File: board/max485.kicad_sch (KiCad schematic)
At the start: 9 parts, among them U1 MAX485E

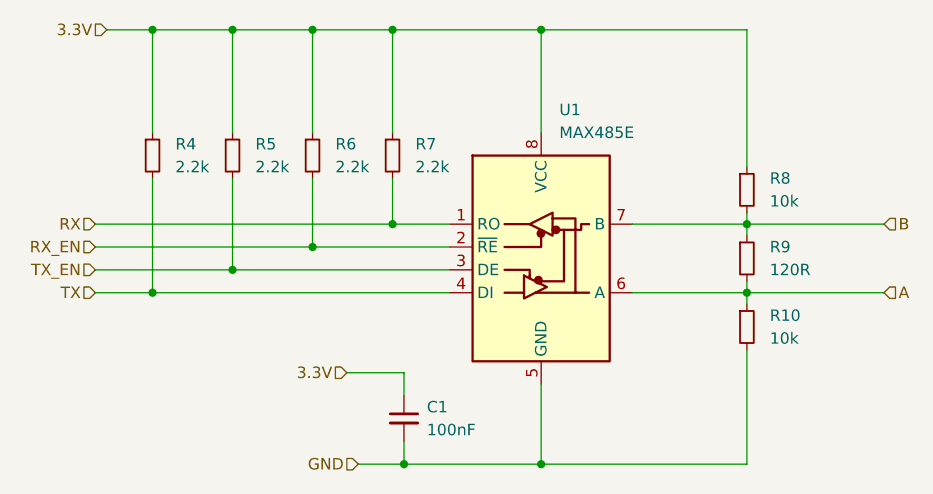
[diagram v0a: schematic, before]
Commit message: changed implementation.kicad_sch to max485.kicad_sch in order to avoid clashing on the name implementation with other edgies in a composition
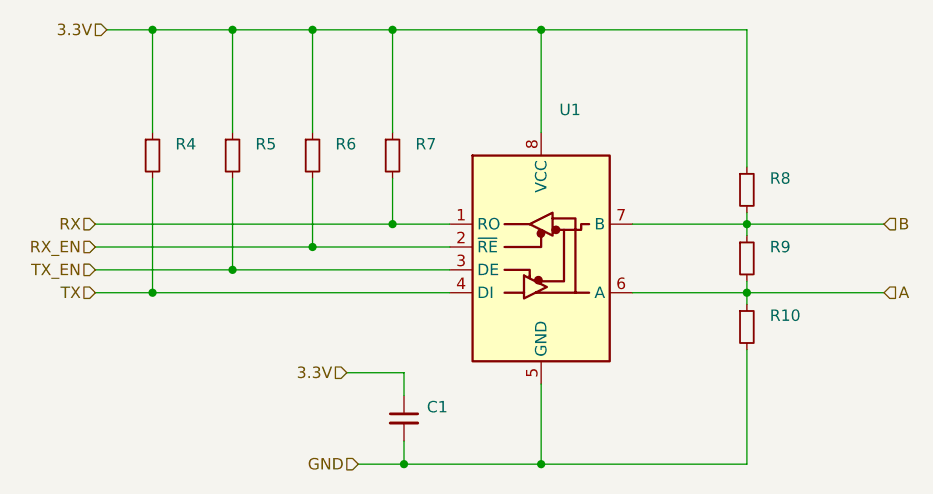
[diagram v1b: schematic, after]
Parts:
- C1: value 100nF -> (none); footprint Resistor_SMD:R_0603_1608Metric -> (none)
- R10, R8: value 10k -> (none); footprint Resistor_SMD:R_0603_1608Metric -> (none)
- R4, R5, R6, R7: value 2.2k -> (none); footprint Resistor_SMD:R_0603_1608Metric -> (none)
- R9: value 120R -> (none); footprint Resistor_SMD:R_0603_1608Metric -> (none)
- U1: value MAX485E -> (none); footprint Package_SO:SO-8_3.9x4.9mm_P1.27mm -> (none)
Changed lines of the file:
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@@
       (effects (font (size 1.27 1.27)) (justify left))
     )
-    (property "Value" "2.2k" (id 1) (at 113.03 91.4399 0)
+    (property "Value" "" (id 1) (at 113.03 91.4399 0)
       (effects (font (size 1.27 1.27)) (justify left))
     )
-    (property "Footprint" "Resistor_SMD:R_0603_1608Metric" (id 2) (at 110.49 90.17 0)
+    (property "Footprint" "" (id 2) (at 110.49 90.17 0)
       (effects (font (size 1.27 1.27)) hide)
     )
@@
       (effects (font (size 1.27 1.27)) (justify left))
     )
-    (property "Value" "100nF" (id 1) (at 123.19 120.6562 0)
+    (property "Value" "" (id 1) (at 123.19 120.6562 0)
       (effects (font (size 1.27 1.27)) (justify left))
     )
-    (property "Footprint" "Resistor_SMD:R_0603_1608Metric" (id 2) (at 120.65 119.38 0)
+    (property "Footprint" "" (id 2) (at 120.65 119.38 0)
       (effects (font (size 1.27 1.27)) hide)
     )
@@
       (effects (font (size 1.27 1.27)) (justify left))
     )
-    (property "Value" "2.2k" (id 1) (at 104.14 91.4399 0)
+    (property "Value" "" (id 1) (at 104.14 91.4399 0)
       (effects (font (size 1.27 1.27)) (justify left))
     )
-    (property "Footprint" "Resistor_SMD:R_0603_1608Metric" (id 2) (at 101.6 90.17 0)
+    (property "Footprint" "" (id 2) (at 101.6 90.17 0)
       (effects (font (size 1.27 1.27)) hide)
     )
@@
       (effects (font (size 1.27 1.27)) (justify left))
     )
-    (property "Value" "120R" (id 1) (at 161.29 102.8699 0)
+    (property "Value" "" (id 1) (at 161.29 102.8699 0)
       (effects (font (size 1.27 1.27)) (justify left))
     )
-    (property "Footprint" "Resistor_SMD:R_0603_1608Metric" (id 2) (at 158.75 101.6 0)
+    (property "Footprint" "" (id 2) (at 158.75 101.6 0)
       (effects (font (size 1.27 1.27)) hide)
     )
@@
       (effects (font (size 1.27 1.27)) (justify left))
     )
-    (property "Value" "10k" (id 1) (at 161.29 110.4899 0)
+    (property "Value" "" (id 1) (at 161.29 110.4899 0)
       (effects (font (size 1.27 1.27)) (justify left))
     )
-    (property "Footprint" "Resistor_SMD:R_0603_1608Metric" (id 2) (at 158.75 109.22 0)
+    (property "Footprint" "" (id 2) (at 158.75 109.22 0)
       (effects (font (size 1.27 1.27)) hide)
     )
@@
       (effects (font (size 1.27 1.27)) (justify left))
     )
-    (property "Value" "2.2k" (id 1) (at 121.92 91.4399 0)
+    (property "Value" "" (id 1) (at 121.92 91.4399 0)
       (effects (font (size 1.27 1.27)) (justify left))
     )
-    (property "Footprint" "Resistor_SMD:R_0603_1608Metric" (id 2) (at 119.38 90.17 0)
+    (property "Footprint" "" (id 2) (at 119.38 90.17 0)
       (effects (font (size 1.27 1.27)) hide)
     )
@@
       (effects (font (size 1.27 1.27)) (justify left))
     )
-    (property "Value" "10k" (id 1) (at 161.29 95.2499 0)
+    (property "Value" "" (id 1) (at 161.29 95.2499 0)
       (effects (font (size 1.27 1.27)) (justify left))
     )
-    (property "Footprint" "Resistor_SMD:R_0603_1608Metric" (id 2) (at 158.75 93.98 0)
+    (property "Footprint" "" (id 2) (at 158.75 93.98 0)
       (effects (font (size 1.27 1.27)) hide)
     )
@@
       (effects (font (size 1.27 1.27)) (justify left))
     )
-    (property "Value" "2.2k" (id 1) (at 95.25 91.4399 0)
+    (property "Value" "" (id 1) (at 95.25 91.4399 0)
       (effects (font (size 1.27 1.27)) (justify left))
     )
-    (property "Footprint" "Resistor_SMD:R_0603_1608Metric" (id 2) (at 92.71 90.17 0)
+    (property "Footprint" "" (id 2) (at 92.71 90.17 0)
       (effects (font (size 1.27 1.27)) hide)
     )
@@
       (effects (font (size 1.27 1.27)) (justify left))
     )
-    (property "Value" "MAX485E" (id 1) (at 137.9094 87.63 0)
+    (property "Value" "" (id 1) (at 137.9094 87.63 0)
       (effects (font (size 1.27 1.27)) (justify left))
     )
-    (property "Footprint" "Package_SO:SO-8_3.9x4.9mm_P1.27mm" (id 2) (at 135.89 118.11 0)
+    (property "Footprint" "" (id 2) (at 135.89 118.11 0)
       (effects (font (size 1.27 1.27)) hide)
     )

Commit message: changed supply to 5V and fixed up silkscreen
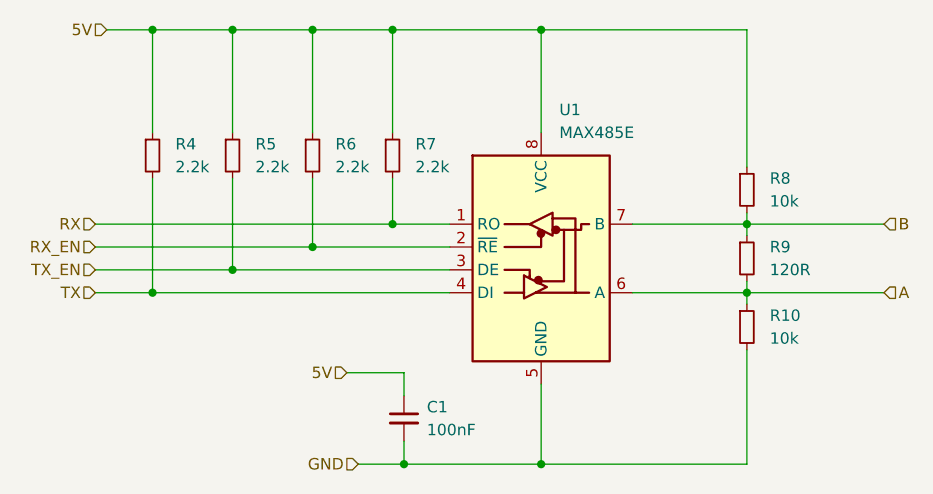
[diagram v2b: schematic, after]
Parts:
- C1: value (none) -> 100nF; footprint (none) -> Capacitor_SMD:C_0603_1608Metric
- R10, R8: value (none) -> 10k; footprint (none) -> Resistor_SMD:R_0603_1608Metric
- R4, R5, R6, R7: value (none) -> 2.2k; footprint (none) -> Resistor_SMD:R_0603_1608Metric
- R9: value (none) -> 120R; footprint (none) -> Resistor_SMD:R_0603_1608Metric
- U1: value (none) -> MAX485E; footprint (none) -> Package_SO:SO-8_3.9x4.9mm_P1.27mm
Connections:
- net 3.3V renamed 5V
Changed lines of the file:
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@@
     (stroke (width 0) (type default) (color 0 0 0 0))
   )
-  (hierarchical_label "3.3V" (shape input) (at 114.3 114.3 180)
+  (hierarchical_label "5V" (shape input) (at 114.3 114.3 180)
     (effects (font (size 1.27 1.27)) (justify right))
   )
@@
     (effects (font (size 1.27 1.27)) (justify right))
   )
-  (hierarchical_label "3.3V" (shape input) (at 87.63 76.2 180)
+  (hierarchical_label "5V" (shape input) (at 87.63 76.2 180)
     (effects (font (size 1.27 1.27)) (justify right))
   )
@@
       (effects (font (size 1.27 1.27)) (justify left))
     )
-    (property "Value" "" (id 1) (at 113.03 91.4399 0)
+    (property "Value" "2.2k" (id 1) (at 113.03 91.4399 0)
       (effects (font (size 1.27 1.27)) (justify left))
     )
-    (property "Footprint" "" (id 2) (at 110.49 90.17 0)
+    (property "Footprint" "Resistor_SMD:R_0603_1608Metric" (id 2) (at 110.49 90.17 0)
       (effects (font (size 1.27 1.27)) hide)
     )
@@
       (effects (font (size 1.27 1.27)) (justify left))
     )
-    (property "Value" "" (id 1) (at 123.19 120.6562 0)
+    (property "Value" "100nF" (id 1) (at 123.19 120.6562 0)
       (effects (font (size 1.27 1.27)) (justify left))
     )
-    (property "Footprint" "" (id 2) (at 120.65 119.38 0)
+    (property "Footprint" "Capacitor_SMD:C_0603_1608Metric" (id 2) (at 120.65 119.38 0)
       (effects (font (size 1.27 1.27)) hide)
     )
@@
       (effects (font (size 1.27 1.27)) (justify left))
     )
-    (property "Value" "" (id 1) (at 104.14 91.4399 0)
+    (property "Value" "2.2k" (id 1) (at 104.14 91.4399 0)
       (effects (font (size 1.27 1.27)) (justify left))
     )
-    (property "Footprint" "" (id 2) (at 101.6 90.17 0)
+    (property "Footprint" "Resistor_SMD:R_0603_1608Metric" (id 2) (at 101.6 90.17 0)
       (effects (font (size 1.27 1.27)) hide)
     )
@@
       (effects (font (size 1.27 1.27)) (justify left))
     )
-    (property "Value" "" (id 1) (at 161.29 102.8699 0)
+    (property "Value" "120R" (id 1) (at 161.29 102.8699 0)
       (effects (font (size 1.27 1.27)) (justify left))
     )
-    (property "Footprint" "" (id 2) (at 158.75 101.6 0)
+    (property "Footprint" "Resistor_SMD:R_0603_1608Metric" (id 2) (at 158.75 101.6 0)
       (effects (font (size 1.27 1.27)) hide)
     )
@@
       (effects (font (size 1.27 1.27)) (justify left))
     )
-    (property "Value" "" (id 1) (at 161.29 110.4899 0)
+    (property "Value" "10k" (id 1) (at 161.29 110.4899 0)
       (effects (font (size 1.27 1.27)) (justify left))
     )
-    (property "Footprint" "" (id 2) (at 158.75 109.22 0)
+    (property "Footprint" "Resistor_SMD:R_0603_1608Metric" (id 2) (at 158.75 109.22 0)
       (effects (font (size 1.27 1.27)) hide)
     )
@@
       (effects (font (size 1.27 1.27)) (justify left))
     )
-    (property "Value" "" (id 1) (at 121.92 91.4399 0)
+    (property "Value" "2.2k" (id 1) (at 121.92 91.4399 0)
       (effects (font (size 1.27 1.27)) (justify left))
     )
-    (property "Footprint" "" (id 2) (at 119.38 90.17 0)
+    (property "Footprint" "Resistor_SMD:R_0603_1608Metric" (id 2) (at 119.38 90.17 0)
       (effects (font (size 1.27 1.27)) hide)
     )
@@
       (effects (font (size 1.27 1.27)) (justify left))
     )
-    (property "Value" "" (id 1) (at 161.29 95.2499 0)
+    (property "Value" "10k" (id 1) (at 161.29 95.2499 0)
       (effects (font (size 1.27 1.27)) (justify left))
     )
-    (property "Footprint" "" (id 2) (at 158.75 93.98 0)
+    (property "Footprint" "Resistor_SMD:R_0603_1608Metric" (id 2) (at 158.75 93.98 0)
       (effects (font (size 1.27 1.27)) hide)
     )
@@
       (effects (font (size 1.27 1.27)) (justify left))
     )
-    (property "Value" "" (id 1) (at 95.25 91.4399 0)
+    (property "Value" "2.2k" (id 1) (at 95.25 91.4399 0)
       (effects (font (size 1.27 1.27)) (justify left))
     )
-    (property "Footprint" "" (id 2) (at 92.71 90.17 0)
+    (property "Footprint" "Resistor_SMD:R_0603_1608Metric" (id 2) (at 92.71 90.17 0)
       (effects (font (size 1.27 1.27)) hide)
     )
@@
       (effects (font (size 1.27 1.27)) (justify left))
     )
-    (property "Value" "" (id 1) (at 137.9094 87.63 0)
+    (property "Value" "MAX485E" (id 1) (at 137.9094 87.63 0)
       (effects (font (size 1.27 1.27)) (justify left))
     )
-    (property "Footprint" "" (id 2) (at 135.89 118.11 0)
+    (property "Footprint" "Package_SO:SO-8_3.9x4.9mm_P1.27mm" (id 2) (at 135.89 118.11 0)
       (effects (font (size 1.27 1.27)) hide)
     )
